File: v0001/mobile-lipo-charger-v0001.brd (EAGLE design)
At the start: 83 x 93.5 mm, 48 parts, among them IC1 AD8610MR, IC2 STM32F401VBT, IC3 AD8610MR, SW1 DHT-4235A, U3 3.3V

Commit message: Reroute
Rerouted some traces to the bottom layer
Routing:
- net I_POT_SDO: track 14.3 -> 16.0 mm, vias 0 -> 2
- net I_POT_SCLK: track 17.1 -> 18.7 mm
- net I_POT_SDI: track 13.8 -> 15.0 mm, vias 0 -> 2
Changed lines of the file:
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@@
 <layer number="17" name="Pads" color="2" fill="1" visible="yes" active="yes"/>
 <layer number="18" name="Vias" color="2" fill="1" visible="yes" active="yes"/>
-<layer number="19" name="Unrouted" color="6" fill="1" visible="no" active="yes"/>
+<layer number="19" name="Unrouted" color="6" fill="1" visible="yes" active="yes"/>
 <layer number="20" name="Dimension" color="24" fill="1" visible="yes" active="yes"/>
 <layer number="21" name="tPlace" color="7" fill="1" visible="yes" active="yes"/>
@@
 <contactref element="U$1" pad="13"/>
 <contactref element="IC2" pad="30"/>
-<via x="38.481" y="86.106" extent="1-16" drill="0.35"/>
-<wire x1="38.481" y1="86.106" x2="36.449" y2="86.106" width="0.254" layer="16"/>
-<wire x1="36.449" y1="86.106" x2="36.195" y2="86.36" width="0.254" layer="16"/>
+<wire x1="36.195" y1="86.36" x2="36.449" y2="86.106" width="0.254" layer="16"/>
 <via x="36.195" y="86.36" extent="1-16" drill="0.35"/>
 <wire x1="36.195" y1="87.249" x2="36.195" y2="86.36" width="0.254" layer="1"/>
 <wire x1="36.393" y1="89.987" x2="36.393" y2="87.447" width="0.254" layer="1"/>
 <wire x1="36.393" y1="87.447" x2="36.195" y2="87.249" width="0.254" layer="1"/>
-<wire x1="34.39610625" y1="76.841434375" x2="38.481" y2="80.926328125" width="0.254" layer="1"/>
-<wire x1="38.481" y1="80.926328125" x2="38.481" y2="86.106" width="0.254" layer="1"/>
+<wire x1="36.449" y1="86.106" x2="37.084" y2="85.471" width="0.3048" layer="16"/>
+<wire x1="37.084" y1="82.296" x2="37.211" y2="82.169" width="0.3048" layer="16"/>
+<wire x1="37.211" y1="82.169" x2="37.211" y2="81.407" width="0.3048" layer="16"/>
+<wire x1="37.211" y1="81.407" x2="32.639" y2="76.835" width="0.3048" layer="16"/>
+<wire x1="32.639" y1="76.835" x2="32.639" y2="75.946" width="0.3048" layer="16"/>
+<via x="32.639" y="75.946" extent="1-16" drill="0.35"/>
+<wire x1="32.766" y1="75.819" x2="32.639" y2="75.946" width="0.3048" layer="1"/>
+<wire x1="37.084" y1="85.471" x2="37.084" y2="82.296" width="0.3048" layer="16"/>
+<wire x1="34.39610625" y1="76.841434375" x2="33.373671875" y2="75.819" width="0.3048" layer="1"/>
+<wire x1="33.373671875" y1="75.819" x2="32.766" y2="75.819" width="0.3048" layer="1"/>
 </signal>
 <signal name="I_POT_SDI">
 <contactref element="U$1" pad="14"/>
 <contactref element="IC2" pad="32"/>
-<wire x1="33.689" y1="77.548540625" x2="37.043" y2="80.902540625" width="0.254" layer="1"/>
-<wire x1="37.043" y1="80.902540625" x2="37.043" y2="89.987" width="0.254" layer="1"/>
+<wire x1="33.689" y1="77.548540625" x2="36.404459375" y2="80.264" width="0.3048" layer="1"/>
+<via x="37.338" y="80.264" extent="1-16" drill="0.35"/>
+<wire x1="37.338" y1="80.264" x2="37.846" y2="80.772" width="0.3048" layer="16"/>
+<wire x1="37.846" y1="82.55" x2="37.719" y2="82.677" width="0.3048" layer="16"/>
+<wire x1="37.719" y1="86.233" x2="37.084" y2="86.868" width="0.3048" layer="16"/>
+<via x="37.084" y="86.868" extent="1-16" drill="0.35"/>
+<wire x1="36.404459375" y1="80.264" x2="37.338" y2="80.264" width="0.3048" layer="1"/>
+<wire x1="37.846" y1="80.772" x2="37.846" y2="82.55" width="0.3048" layer="16"/>
+<wire x1="37.719" y1="82.677" x2="37.719" y2="86.233" width="0.3048" layer="16"/>
+<wire x1="37.043" y1="89.987" x2="37.084" y2="89.946" width="0.3048" layer="1"/>
+<wire x1="37.084" y1="89.946" x2="37.084" y2="86.868" width="0.3048" layer="1"/>
 </signal>
 <signal name="N$4">
@@
 <contactref element="U$1" pad="15"/>
 <contactref element="IC2" pad="31"/>
-<wire x1="34.042553125" y1="77.1949875" x2="37.693" y2="80.845434375" width="0.254" layer="1"/>
-<wire x1="37.693" y1="80.845434375" x2="37.693" y2="89.987" width="0.254" layer="1"/>
+<wire x1="34.042553125" y1="77.1949875" x2="36.095565625" y2="79.248" width="0.3048" layer="1"/>
+<via x="37.338" y="79.248" extent="1-16" drill="0.35"/>
+<wire x1="37.338" y1="79.248" x2="37.465" y2="79.375" width="0.3048" layer="16"/>
+<wire x1="37.465" y1="79.375" x2="37.973" y2="79.375" width="0.3048" layer="16"/>
+<wire x1="37.973" y1="79.375" x2="38.481" y2="79.883" width="0.3048" layer="16"/>
+<wire x1="38.481" y1="82.804" x2="38.354" y2="82.931" width="0.3048" layer="16"/>
+<wire x1="38.354" y1="86.995" x2="37.846" y2="87.503" width="0.3048" layer="16"/>
+<via x="37.846" y="87.503" extent="1-16" drill="0.35"/>
+<wire x1="37.719" y1="87.63" x2="37.846" y2="87.503" width="0.3048" layer="1"/>
+<wire x1="36.095565625" y1="79.248" x2="37.338" y2="79.248" width="0.3048" layer="1"/>
+<wire x1="38.481" y1="79.883" x2="38.481" y2="82.804" width="0.3048" layer="16"/>
+<wire x1="38.354" y1="82.931" x2="38.354" y2="86.995" width="0.3048" layer="16"/>
+<wire x1="37.693" y1="89.987" x2="37.719" y2="89.961" width="0.3048" layer="1"/>
+<wire x1="37.719" y1="89.961" x2="37.719" y2="87.63" width="0.3048" layer="1"/>
 </signal>
 <signal name="VBAT">

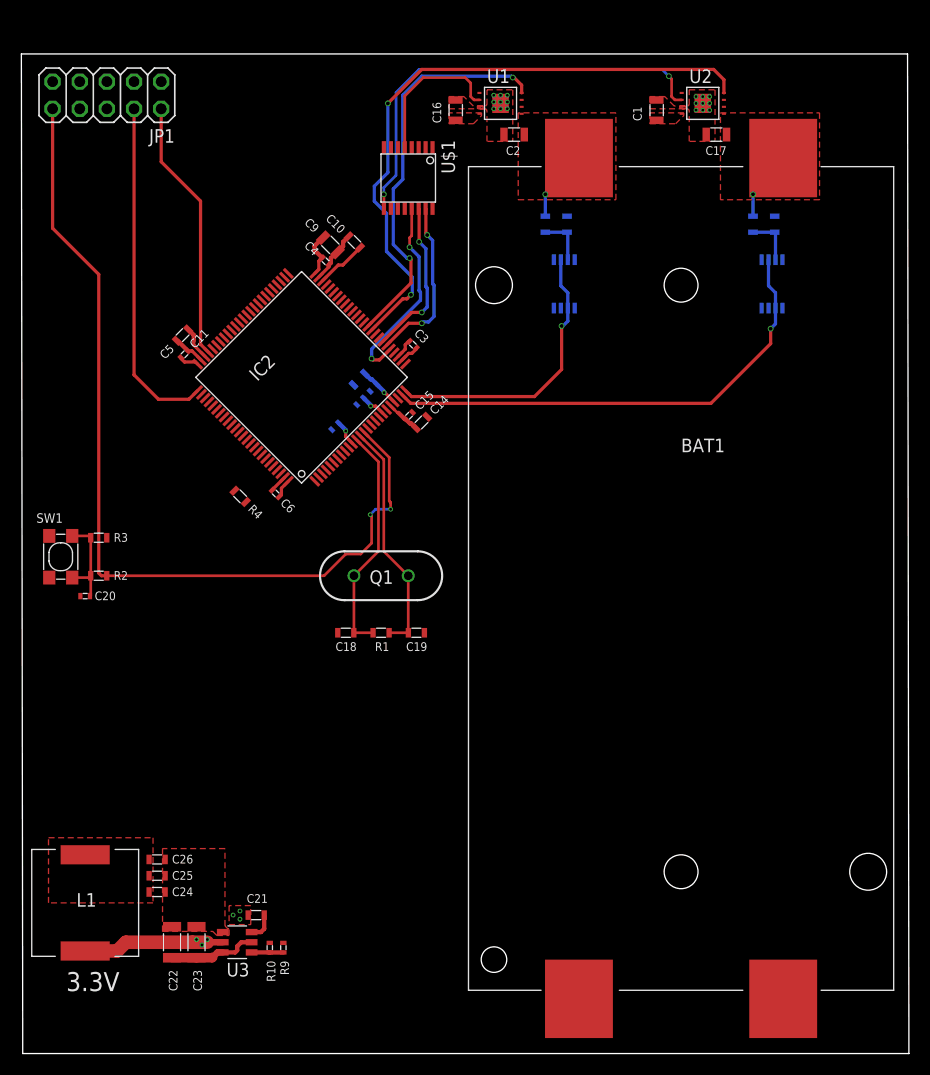
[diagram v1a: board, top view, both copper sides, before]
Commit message: Added new routes
Added routes form CHARGE and DONE lines of both charger chips.
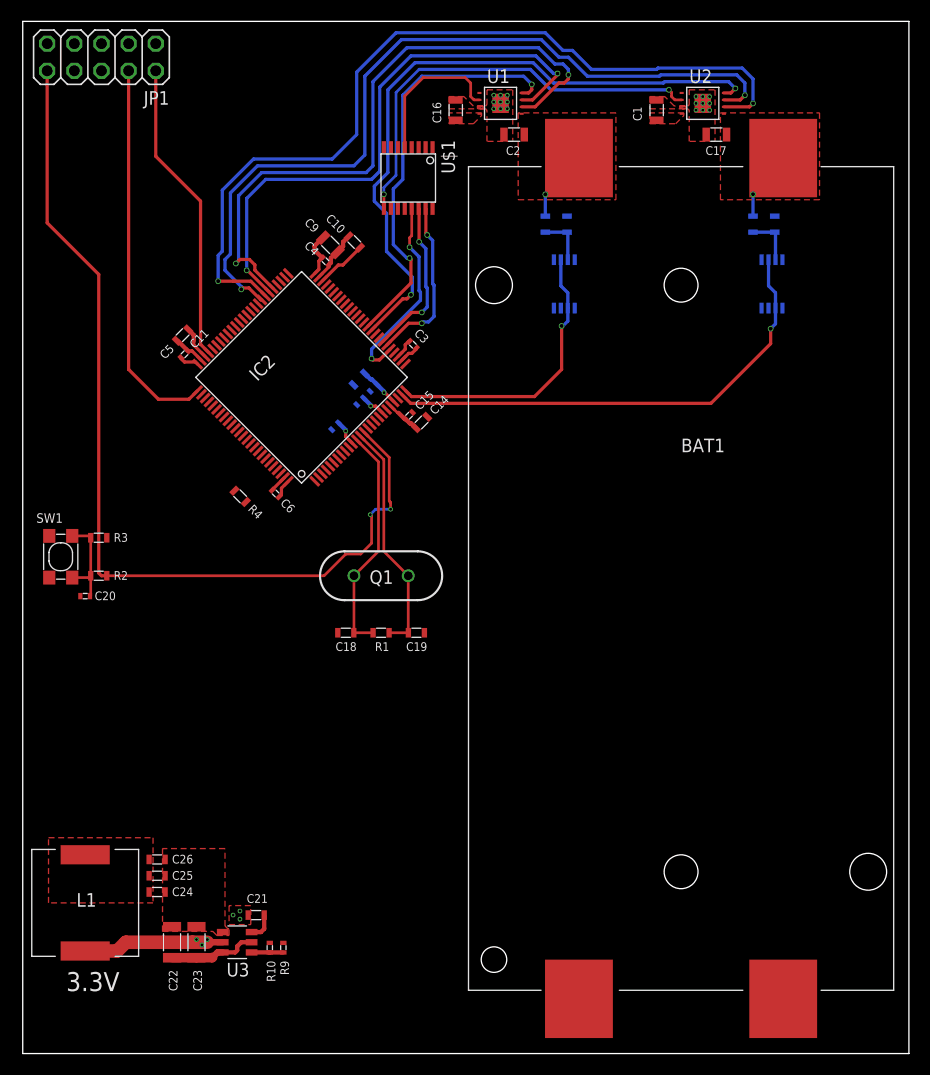
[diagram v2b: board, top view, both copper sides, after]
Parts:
- moved JP1 3.59 mm to (7.37, 104.1)
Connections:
- net BATT1_CHARGE: now also IC2.56
- net BATT1_DONE: now also IC2.55
- net BATT2_CHARGE: now also IC2.58
- net BATT2_DONE: now also IC2.57
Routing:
- net BATT2_DONE: track 0.00 -> 79.9 mm, vias 0 -> 2
- net BATT2_CHARGE: track 0.00 -> 75.8 mm, vias 0 -> 2
- net BATT1_DONE: track 0.00 -> 59.9 mm, vias 0 -> 2
- net BATT1_CHARGE: track 0.00 -> 54.1 mm, vias 0 -> 2
- net TMS_SWDIO: track 24.7 -> 28.4 mm
- net RST: track 85.2 -> 89.0 mm
- net TCK_SWCLK: track 32.1 -> 35.9 mm
- net BATT2_CE: track 59.4 -> 62.2 mm
- net BATT1_CE: track 37.4 -> 39.2 mm
- net BATT2_ISET: track 41.1 -> 40.4 mm
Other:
- board size 83 x 93.5 mm -> 82.9 x 96.6 mm
